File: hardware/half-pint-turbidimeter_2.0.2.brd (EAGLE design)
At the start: 50.8 x 32 mm, 24 parts, among them IC1 MEGA8-AI

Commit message: updating v2.0.2
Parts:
- removed JP7: M01SMD-4.5X1.5, SparkFun-Connectors:PAD-1.5X4.5
- added U$1: ISP-SMD-6PIN, awqua_eagle_library:ISP-SMD-6PIN
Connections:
- net GND: now also U$1.P6
- net MISO: now also U$1.P1
- net MOSI: now also U$1.P4
- net RST: now also U$1.P5; no longer JP7.P$1
- net SCK: now also U$1.P3
- net VCC: now also U$1.P2
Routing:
- net GND: track 60.0 -> 92.0 mm, vias 0 -> 2
- net SCK: track 17.8 -> 41.9 mm, vias 1 -> 2
- net MISO: track 13.6 -> 30.3 mm, vias 1 -> 2
- net INT2: track 35.1 -> 20.8 mm, vias 7 -> 3
- net SDA: track 61.1 -> 70.0 mm, vias 3 -> 0
- net VCC: track 174.2 -> 183.0 mm, vias 15 -> 4
- net BTN3: track 30.3 -> 38.5 mm
- net RX: track 36.1 -> 28.0 mm, vias 2 -> 1
- net SCL: track 53.7 -> 60.6 mm, vias 5 -> 2
- net CS: track 20.7 -> 26.6 mm
- net MOSI: track 24.6 -> 19.4 mm, vias 1 -> 2
- net BTN2: track 33.9 -> 38.4 mm, vias 1 -> 0
- net AIN0: track 18.3 -> 22.5 mm, vias 3 -> 1
- net RST: track 45.9 -> 49.8 mm, vias 5 -> 7
- net BTN1: track 27.7 -> 30.2 mm, vias 1 -> 0
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
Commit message: minor edits to eagle schematics
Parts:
- moved FRAME1 9.77 mm to (22.5, -17.3)
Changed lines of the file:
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@@
 <?xml version="1.0" encoding="utf-8"?>
 <!DOCTYPE eagle SYSTEM "eagle.dtd">
-<eagle version="7.2.0">
+<eagle version="7.3.0">
 <drawing>
 <settings>
@@
 <attribute name="VALUE" x="38.1" y="25.781" size="0.4064" layer="25" font="vector"/>
 </element>
-<element name="FRAME1" library="SparkFun-Aesthetics" package="CREATIVE_COMMONS" value="FRAME-LETTER" x="20.955" y="-7.62"/>
+<element name="FRAME1" library="SparkFun-Aesthetics" package="CREATIVE_COMMONS" value="FRAME-LETTER" x="22.479" y="-17.272"/>
 <element name="C6" library="SparkFun" package="0603-CAP" value="100n" x="25.4" y="1.778" smashed="yes" rot="R180">
 <attribute name="VALUE" x="27.559" y="1.524" size="0.4064" layer="25" font="vector" rot="R90"/>

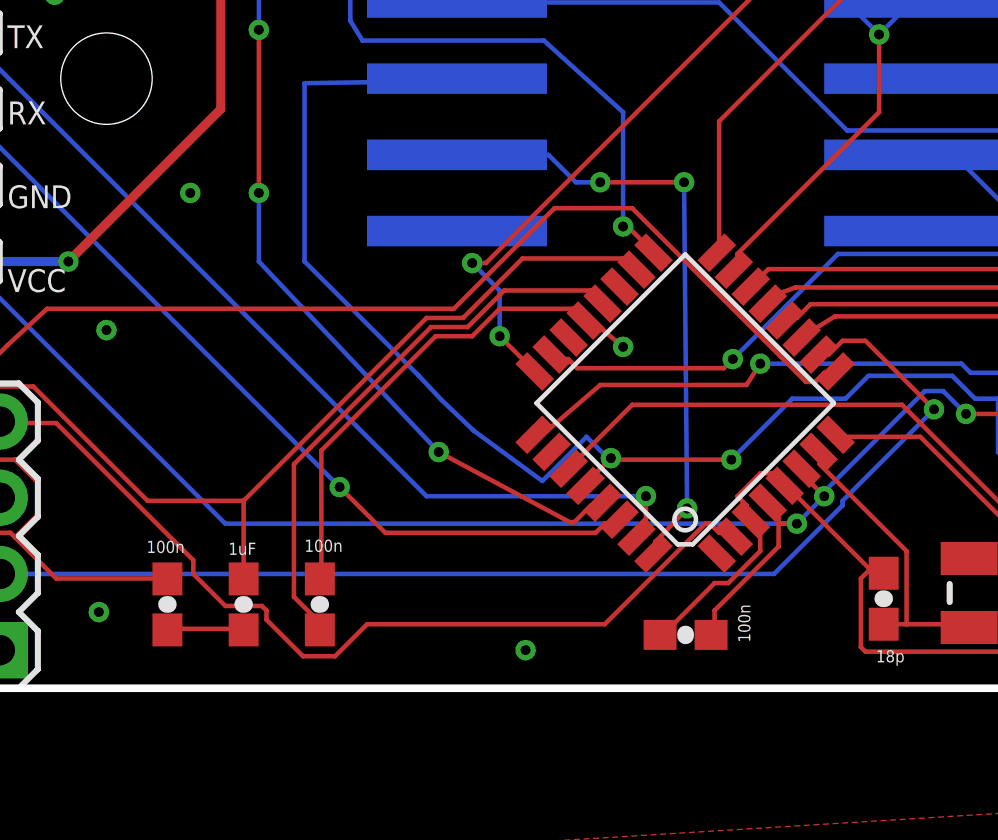
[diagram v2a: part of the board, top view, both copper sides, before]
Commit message: airwire fixed
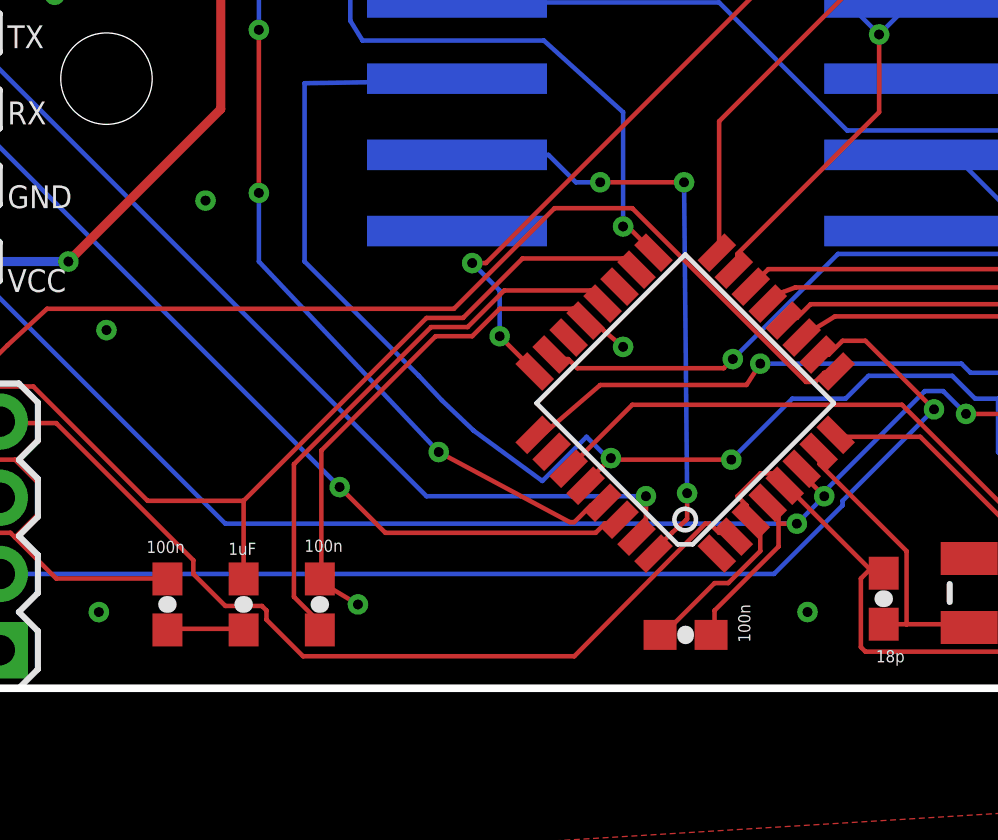
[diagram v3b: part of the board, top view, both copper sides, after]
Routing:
- net GND: track 92.0 -> 93.5 mm, vias 2 -> 3
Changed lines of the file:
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@@
 <wire x1="21.59" y1="27.686" x2="18.034" y2="27.686" width="0.3048" layer="16"/>
 <wire x1="18.034" y1="27.686" x2="17.78" y2="27.94" width="0.3048" layer="16"/>
-<wire x1="13.208" y1="3.644" x2="10.668" y2="1.9812" width="0" layer="19" extent="1-1"/>
+<wire x1="13.208" y1="3.644" x2="13.208" y2="3.556" width="0.1524" layer="1"/>
+<wire x1="13.208" y1="3.556" x2="14.478" y2="2.794" width="0.1524" layer="1"/>
+<via x="14.478" y="2.794" extent="1-16" drill="0.3302"/>
 </signal>
 <signal name="VCC">
@@
 <contactref element="JP11" pad="5"/>
 <contactref element="IC1" pad="32"/>
-<wire x1="24.384" y1="4.8768" x2="24.384" y2="4.572" width="0.1524" layer="1"/>
-<wire x1="24.6888" y1="5.1816" x2="24.384" y2="4.8768" width="0.1524" layer="1"/>
-<wire x1="25.4508" y1="5.9944" x2="24.6888" y2="5.1816" width="0.1524" layer="1"/>
-<wire x1="25.3492" y1="16.8656" x2="25.4508" y2="5.9944" width="0.1524" layer="16"/>
+<wire x1="24.638" y1="4.8768" x2="24.384" y2="4.572" width="0.1524" layer="1"/>
+<wire x1="24.9428" y1="5.1816" x2="24.638" y2="4.8768" width="0.1524" layer="1"/>
+<wire x1="25.4508" y1="6.5024" x2="25.4508" y2="5.6388" width="0.1524" layer="1"/>
+<wire x1="25.4508" y1="5.6388" x2="25.4" y2="5.588" width="0.1524" layer="1"/>
+<wire x1="25.4" y1="5.588" x2="24.9428" y2="5.1816" width="0.1524" layer="1"/>
+<wire x1="25.3492" y1="16.8656" x2="25.4508" y2="6.5024" width="0.1524" layer="16"/>
 <wire x1="22.5552" y1="16.8656" x2="25.3492" y2="16.8656" width="0.1524" layer="1"/>
 <wire x1="19.2024" y1="17.6784" x2="20.828" y2="17.78" width="0.1524" layer="16"/>
@@
 <wire x1="24.384" y1="4.572" x2="24.331078125" y2="4.488278125" width="0.1524" layer="1"/>
 <wire x1="17.8308" y1="17.6784" x2="17.78" y2="17.78" width="0.1524" layer="16"/>
-<via x="25.4508" y="5.9944" extent="1-16" drill="0.3302"/>
+<via x="25.4508" y="6.5024" extent="1-16" drill="0.3302"/>
 <via x="22.5552" y="16.8656" extent="1-16" drill="0.3302"/>
 <via x="25.3492" y="16.8656" extent="1-16" drill="0.3302"/>
@@
 <wire x1="26.2128" y1="5.4864" x2="26.5176" y2="5.1816" width="0.1524" layer="1"/>
 <wire x1="26.0604" y1="5.4864" x2="26.2128" y2="5.4864" width="0.1524" layer="1"/>
-<wire x1="22.7076" y1="2.1336" x2="26.0604" y2="5.4864" width="0.1524" layer="1"/>
-<wire x1="14.7828" y1="2.1336" x2="22.7076" y2="2.1336" width="0.1524" layer="1"/>
-<wire x1="13.716" y1="1.0668" x2="14.7828" y2="2.1336" width="0.1524" layer="1"/>
-<wire x1="12.6492" y1="1.0668" x2="13.716" y2="1.0668" width="0.1524" layer="1"/>
+<wire x1="21.6916" y1="1.0668" x2="26.0604" y2="5.4864" width="0.1524" layer="1"/>
+<wire x1="12.6492" y1="1.0668" x2="21.6916" y2="1.0668" width="0.1524" layer="1"/>
 <wire x1="11.43" y1="2.286" x2="12.6492" y2="1.0668" width="0.1524" layer="1"/>
 <wire x1="11.43" y1="2.5908" x2="11.43" y2="2.286" width="0.1524" layer="1"/>
@@
 </signal>
 <signal name="N$3">
-<via x="20.066" y="1.27" extent="1-16" drill="0.3302"/>
+<via x="29.464" y="2.54" extent="1-16" drill="0.3302"/>
 </signal>
 <signal name="N$4">
@@
 </signal>
 <signal name="N$9">
-<via x="8.89" y="16.51" extent="1-16" drill="0.3302"/>
+<via x="9.398" y="16.256" extent="1-16" drill="0.3302"/>
 </signal>
 </signals>

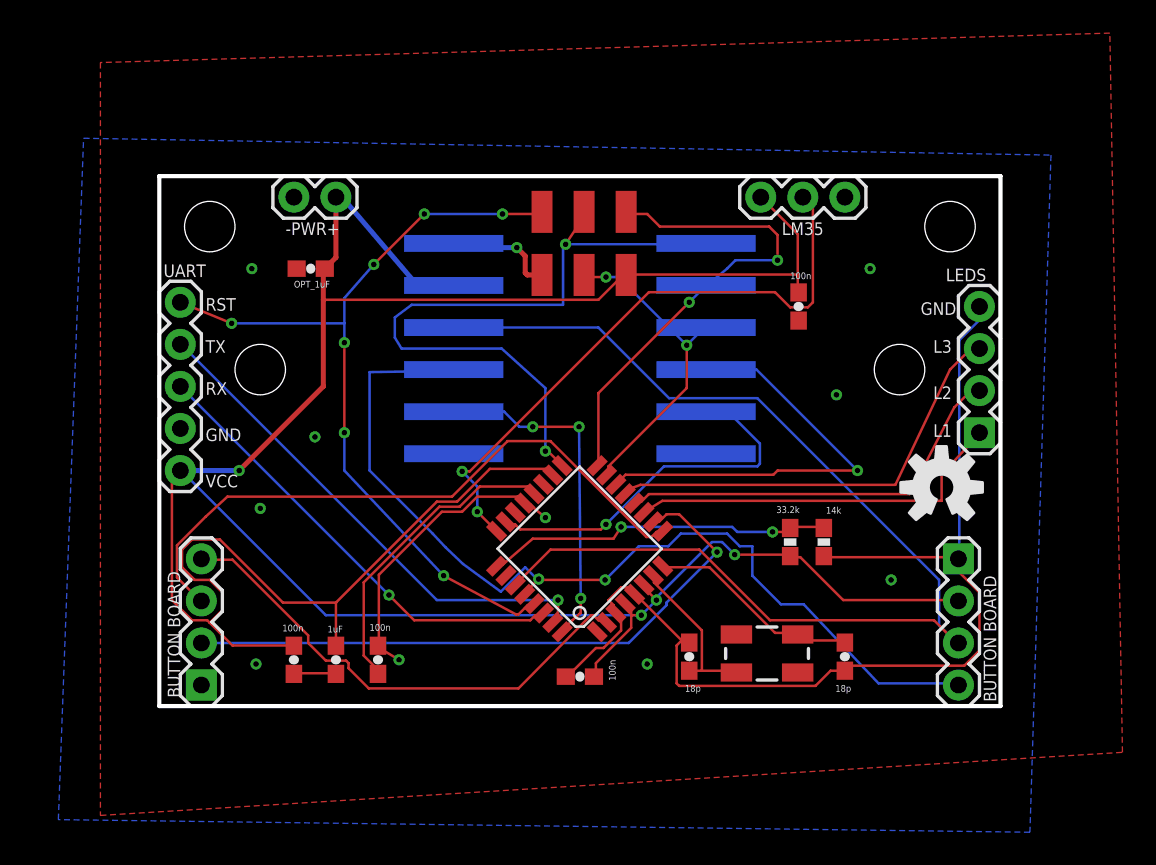
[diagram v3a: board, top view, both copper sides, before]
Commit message: fixed a label, added smd icsp
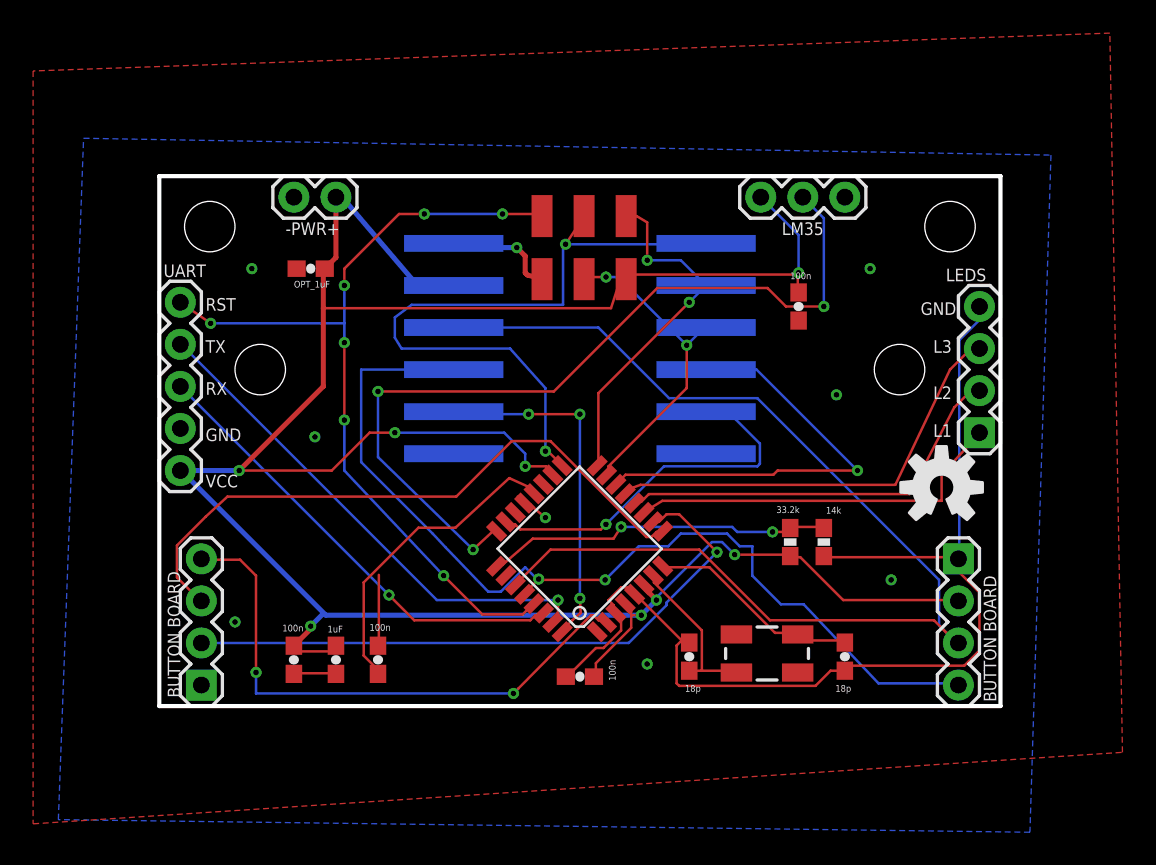
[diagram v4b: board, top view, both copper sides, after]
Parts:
- moved FRAME1 9.77 mm to (21.0, -7.62)
- moved U$1 0.25 mm to (25.7, 27.7)
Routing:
- net VCC: track 183.0 -> 158.5 mm, vias 4 -> 8
- net TEMP: track 37.2 -> 51.0 mm, vias 2 -> 3
- net GND: track 93.5 -> 81.8 mm, vias 3 -> 2
- net MISO: track 30.3 -> 21.7 mm
- net BTN1: track 30.2 -> 34.2 mm, vias 0 -> 2
- net RST: track 49.8 -> 51.3 mm
- net SCL: track 60.6 -> 61.6 mm
- net INT2: track 20.9 -> 21.4 mm
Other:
- board text added: "awqua pocket-turbidimeter V2.0.2 2016/04/01 github.com/awqua"
- board text removed: "awqua pocket-turbidimeter V2.0.1 2016/03/14 github.com/awqua"

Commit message: hardware updates
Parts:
- added JP2, JP7: (no value), SparkFun-Connectors:1X01
- moved Y1 0.25 mm to (36.7, 2.92)
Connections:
- net GND: now also JP2.1, JP7.1
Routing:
- net GND: track 81.8 -> 68.5 mm
- net SCL: track 61.6 -> 62.2 mm
- net VCC: track 158.5 -> 158.0 mm
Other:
- board size 50.8 x 32 mm -> 50.8 x 36.8 mm
- board text added: "GNDs"
- board text added: "awqua pocket-turbidimeter V2.0.3 2016/05/03 github.com/awqua"
- board text removed: "awqua pocket-turbidimeter V2.0.2 2016/04/01 github.com/awqua"
